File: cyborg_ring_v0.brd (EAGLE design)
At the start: 100 x 80 mm, 0 parts

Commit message: Schematic
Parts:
- added C1: 100n, rcl:C0402K
- added GND, MISO, MOSI, RST, SCK, VCC: TPTP20R, testpad:TP20R
- added LED_CON1, LED_CON10, LED_CON11, LED_CON12, LED_CON13, LED_CON14, LED_CON15, LED_CON16, LED_CON2, LED_CON3, LED_CON4, LED_CON5, LED_CON6, LED_CON7, LED_CON8, LED_CON9: R0508-1/2, cyborg_ring:R0508-1/2
- added RCON1, RCON10, RCON11, RCON12, RCON13, RCON14, RCON2, RCON3, RCON4, RCON5, RCON6, RCON7, RCON8, RCON9: R0805-1/2, cyborg_ring:R0805-1/2
- added SW1: (no value), cyborg_ring:BTN_CK_KSS
- added U$1, U$2: BAT+, cyborg_ring:BAT+
- added U$3, U$4: BAT-, cyborg_ring:BAT-
- added U1: ATTINYX5V-LEFT, cyborg_ring:1/4-QFN20
- added U2: ATTINYX5V-RIGHT, cyborg_ring:1/4-QFN20
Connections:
- new net GND: C1.2, GND.TP, RCON11.1, RCON13.1, RCON3.1, RCON5.1, RCON7.1, RCON9.1, SW1.P$2, U$4.P$1
- new net GND1: RCON10.1, RCON12.1, RCON14.1, RCON4.1, RCON6.1, RCON8.1
- new net LEDL_L1: MOSI.TP
- new net LED_L0: LED_CON1.P$1, LED_CON3.P$1, LED_CON5.P$1, LED_CON7.P$1, SCK.TP, U1.4
- new net LED_L1: LED_CON11.P$1, LED_CON13.P$1, LED_CON15.P$1, LED_CON9.P$1, U1.1
- new net LED_R0: LED_CON14.P$1, LED_CON16.P$1, LED_CON2.P$1, LED_CON4.P$1, U2.2
- new net LED_R1: LED_CON10.P$1, LED_CON12.P$1, LED_CON6.P$1, LED_CON8.P$1, U2.5
- new net N$11: U$2.P$1, U$3.P$1
- new net RST: RCON1.1, RST.TP
- new net RST1: RCON2.1, U2.1
- new net SWITCH: MISO.TP, SW1.P$1, U1.2
- new net VCC: C1.1, U$1.P$1, U1.5, VCC.TP
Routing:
- added copper zone on layer 1, net GND
- added copper zone on layer 16, net GND
- added copper zone on layer 1, net GND1
- added copper zone on layer 16, net GND1

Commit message: Board
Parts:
- removed RCON10, RCON3, RCON4, RCON9: R0805-1/2, cyborg_ring:R0805-1/2
- added PAD: TPTP06R, testpad:TP06R
- added RCON15, RCON16: R0805-1/2TEST2, cyborg_ring:R0905-1/2BIS
- C1: device rcl:C0402K -> rcl:C0201
- GND, MISO, MOSI, RST, SCK, VCC: value TPTP20R -> TPTP15R; device testpad:TP20R -> testpad:TP15R
- RCON1, RCON11, RCON12, RCON13, RCON14, RCON2, RCON7, RCON8: value R0805-1/2 -> R0805-1/2TEST
- RCON5, RCON6: value R0805-1/2 -> R0805-1/2TEST2; device cyborg_ring:R0805-1/2 -> cyborg_ring:R0905-1/2BIS
- moved RCON6 84.2 mm to (24.6, 7.05), turned to 105 degrees
- moved LED_CON2 76.1 mm to (25.4, 19.8), turned to 315.5 degrees
- moved VCC 74.9 mm to (5.14, 2.71), flipped to the bottom
- moved RCON12 73.1 mm to (24.4, 18.3), turned to 75 degrees
- moved LED_CON4 72.3 mm to (27.2, 21.2), turned to 302.5 degrees
- moved RST 71.2 mm to (7.68, 2.71), flipped to the bottom
- moved LED_CON6 69.1 mm to (29.3, 22.2), turned to 289.5 degrees
- moved SCK 67.7 mm to (10.2, 2.71), flipped to the bottom
- moved RCON14 67.2 mm to (29.4, 2.69), turned to 90 degrees
- moved LED_CON8 66.1 mm to (31.5, 22.7), turned to 276.5 degrees
- moved MISO 64.9 mm to (15.3, 2.71), flipped to the bottom
- moved LED_CON10 63.3 mm to (33.7, 22.7), turned to 263.5 degrees
- moved LED_CON12 60.8 mm to (35.9, 22.1), turned to 250.5 degrees
- moved MOSI 60.6 mm to (12.8, 2.71), flipped to the bottom
- moved U$2 58.8 mm to (25.4, 3.40)
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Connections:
- removed net LEDL_L1: MOSI.TP
- removed net LED_L0: LED_CON1.P$1, LED_CON3.P$1, LED_CON5.P$1, LED_CON7.P$1, SCK.TP, U1.4
- removed net LED_L1: LED_CON11.P$1, LED_CON13.P$1, LED_CON15.P$1, LED_CON9.P$1, U1.1
- removed net LED_R0: LED_CON14.P$1, LED_CON16.P$1, LED_CON2.P$1, LED_CON4.P$1, U2.2
- removed net LED_R1: LED_CON10.P$1, LED_CON12.P$1, LED_CON6.P$1, LED_CON8.P$1, U2.5
- removed net N$11: U$2.P$1, U$3.P$1
- removed net SWITCH: MISO.TP, SW1.P$1, U1.2
- new net MISO/SW: MISO.TP, RCON13.1, U1.4
- new net MOSI/L1: LED_CON1.P$1, LED_CON3.P$1, LED_CON5.P$1, LED_CON7.P$1, MOSI.TP, U1.5
- new net R0: LED_CON14.P$1, LED_CON16.P$1, LED_CON2.P$1, LED_CON4.P$1, U2.4
- new net R1: LED_CON10.P$1, LED_CON12.P$1, LED_CON6.P$1, LED_CON8.P$1, U2.1
- new net SCK/L0: LED_CON11.P$1, LED_CON13.P$1, LED_CON15.P$1, LED_CON9.P$1, SCK.TP, U1.2
- new net SWITCH1: RCON14.1, SW1.P$2
- new net VCC": RCON16.1, RCON8.1
- new net VCC/2: RCON6.1, U$2.P$1, U$3.P$1
- new net VCC/2": RCON5.1
- net GND: now also PAD.TP; no longer RCON13.1, RCON3.1, RCON5.1, RCON7.1, RCON9.1, SW1.P$2
- net GND1: now also SW1.P$1; no longer RCON10.1, RCON14.1, RCON4.1, RCON6.1, RCON8.1
- net RST1: now also U2.5; no longer U2.1
- net VCC: now also RCON15.1, RCON7.1, U1.1; no longer U1.5
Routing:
- net R0: track 0.00 -> 36.6 mm, vias 0 -> 3
- net SCK/L0: track 0.00 -> 21.1 mm, vias 0 -> 2
- net R1: track 0.00 -> 21.0 mm, vias 0 -> 2
- net MOSI/L1: track 0.00 -> 20.6 mm, vias 0 -> 2
- net MISO/SW: track 0.00 -> 4.32 mm, vias 0 -> 1
- net N$20: track 0.00 -> 3.05 mm
- net N$23: track 0.00 -> 2.54 mm
- net N$13: track 0.00 -> 2.54 mm
- net N$16: track 0.00 -> 2.54 mm
- net N$18: track 0.00 -> 2.54 mm
- net RST1: track 0.00 -> 2.47 mm
- net N$22: track 0.00 -> 2.45 mm
- net N$21: track 0.00 -> 2.03 mm
- net N$3: track 0.00 -> 2.03 mm
- net N$2: track 0.00 -> 2.03 mm
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- added copper zone on layer 1, net MOSI/L1
- added copper zone on layer 1, net R0
- added copper zone on layer 1, net R1
- added copper zone on layer 1, net SCK/L0
- added copper zone on layer 1, net VCC"
- added copper zone on layer 1, net VCC
- added copper zone on layer 1, net VCC/2"
- added copper zone on layer 1, net VCC/2
- removed copper zone on layer 1, net GND1
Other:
- board size 100 x 80 mm -> 41.8 x 24 mm

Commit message: Clean files
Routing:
- net N$13: track 2.54 -> 0.00 mm
- net N$16: track 2.54 -> 0.00 mm
- net N$18: track 2.54 -> 0.00 mm
- net N$14: track 1.02 -> 0.00 mm
- net N$17: track 1.02 -> 0.00 mm
- net N$15: track 1.02 -> 0.00 mm
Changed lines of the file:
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@@
 <wire x1="39.337309375" y1="3.10610625" x2="40.353309375" y2="3.10610625" width="0.4064" layer="16"/>
-</signal>
-<signal name="N$13">
-<wire x1="11.503678125" y1="23.241846875" x2="10.99568125" y2="23.2409625" width="0.254" layer="16"/>
-<wire x1="10.99568125" y1="23.2409625" x2="10.996565625" y2="22.7329625" width="0.254" layer="16"/>
-<wire x1="11.504565625" y1="22.73385" x2="10.996565625" y2="22.7329625" width="0.254" layer="16"/>
-<wire x1="10.996565625" y1="22.7329625" x2="10.997453125" y2="22.2249625" width="0.254" layer="16"/>
-<wire x1="10.997453125" y1="22.2249625" x2="11.505453125" y2="22.22585" width="0.254" layer="16"/>
-</signal>
-<signal name="N$14">
-<wire x1="9.7809625" y1="23.118596875" x2="9.915334375" y2="22.111521875" width="0.254" layer="16"/>
-</signal>
-<signal name="N$15">
-<wire x1="8.213396875" y1="22.808596875" x2="8.47806875" y2="21.827678125" width="0.254" layer="16"/>
-</signal>
-<signal name="N$16">
-<wire x1="7.384046875" y1="22.513078125" x2="6.91505625" y2="22.31785625" width="0.254" layer="16"/>
-<wire x1="6.91505625" y1="22.31785625" x2="7.110278125" y2="21.848865625" width="0.254" layer="16"/>
-<wire x1="7.110278125" y1="21.848865625" x2="7.57926875" y2="22.0440875" width="0.254" layer="16"/>
-<wire x1="7.57926875" y1="22.0440875" x2="7.774490625" y2="21.575096875" width="0.254" layer="16"/>
-<wire x1="7.774490625" y1="21.575096875" x2="7.3055" y2="21.379875" width="0.254" layer="16"/>
-</signal>
-<signal name="N$17">
-<wire x1="5.710884375" y1="21.60916875" x2="6.22041875" y2="20.730175" width="0.254" layer="16"/>
-</signal>
-<signal name="N$18">
-<wire x1="4.96215" y1="21.1293625" x2="4.559665625" y2="20.819409375" width="0.254" layer="16"/>
-<wire x1="4.559665625" y1="20.819409375" x2="4.86961875" y2="20.416925" width="0.254" layer="16"/>
-<wire x1="4.86961875" y1="20.416925" x2="5.272103125" y2="20.726878125" width="0.254" layer="16"/>
-<wire x1="5.272103125" y1="20.726878125" x2="5.58205625" y2="20.324396875" width="0.254" layer="16"/>
-<wire x1="5.58205625" y1="20.324396875" x2="5.179575" y2="20.01444375" width="0.254" layer="16"/>
 </signal>
 <signal name="N$19">

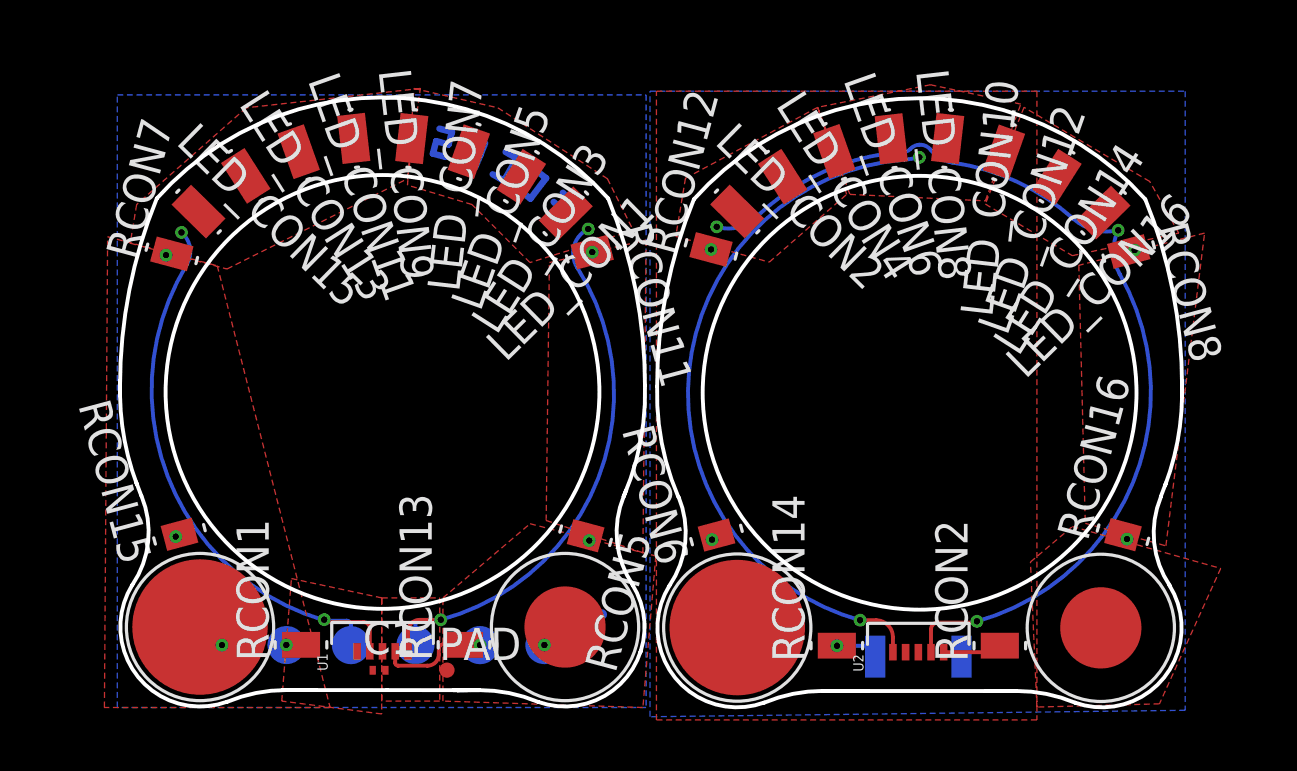
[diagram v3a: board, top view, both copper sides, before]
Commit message: Clearer schematic
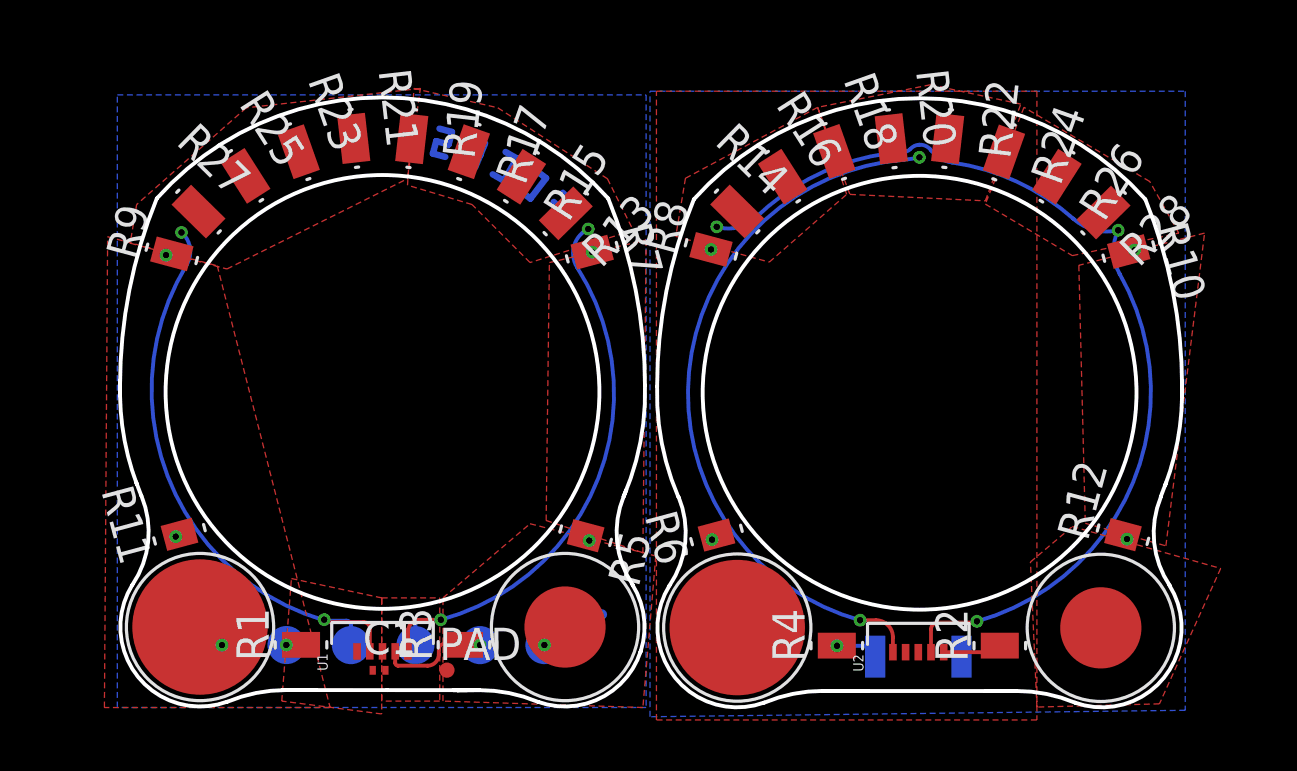
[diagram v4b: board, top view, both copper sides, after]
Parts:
- renumbered LED_CON1 to R13, LED_CON10 to R22, LED_CON11 to R23, LED_CON12 to R24, LED_CON13 to R25, LED_CON14 to R26, LED_CON15 to R27, LED_CON16 to R28, LED_CON2 to R14, LED_CON3 to R15, LED_CON4 to R16, LED_CON5 to R17, LED_CON6 to R18, LED_CON7 to R19, LED_CON8 to R20, LED_CON9 to R21, RCON1 to R1, RCON11 to R7, RCON12 to R8, RCON13 to R3, RCON14 to R4, RCON15 to R11, RCON16 to R12, RCON2 to R2, RCON5 to R5, RCON6 to R6, RCON7 to R9, RCON8 to R10
